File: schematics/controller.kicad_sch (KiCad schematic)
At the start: 48 parts, among them J1 Conn_LoadCell, J2 Conn_Display, J3 Conn_UART, J4 Conn_LiPo, P1 USB-C-6Pin, Q1 MMBT4403, Q2 IRLML6402, SW1 SW_EN, SW2 SW_Boot, SW3 RotaryEncoder_Switch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

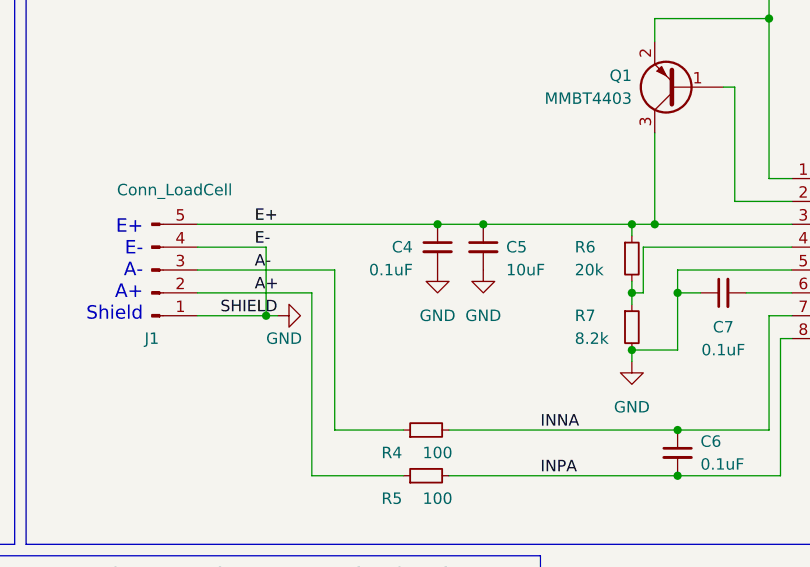
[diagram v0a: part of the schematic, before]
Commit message: Updated voltage divider for hx711 in schematic
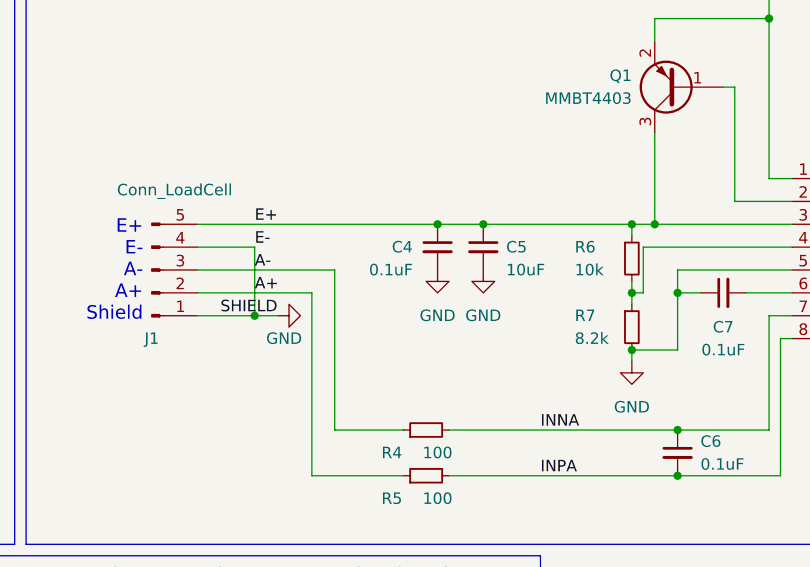
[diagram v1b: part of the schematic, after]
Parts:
- R6: value 20k -> 10k
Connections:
- net A+ is gone; now on net GND: J1.2 (Pin_2), R5.1
- net A- is gone; now on net GND: J1.3 (Pin_3), R4.1
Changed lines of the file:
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@@
   (junction (at 237.49 195.58) (diameter 0) (color 0 0 0 0)
   )
+  (junction (at 214.63 132.08) (diameter 0) (color 0 0 0 0)
+  )
   (junction (at 256.54 129.54) (diameter 0) (color 0 0 0 0)
   )
@@
   )
   (junction (at 308.61 121.92) (diameter 0) (color 0 0 0 0)
-  )
-  (junction (at 215.9 132.08) (diameter 0) (color 0 0 0 0)
   )
   (junction (at 142.24 245.11) (diameter 0) (color 0 0 0 0)
@@
     (stroke (width 0) (type default) (color 0 0 0 0))
   )
+  (wire (pts (xy 214.63 132.08) (xy 217.17 132.08))
+    (stroke (width 0) (type default) (color 0 0 0 0))
+  )
   (polyline (pts (xy 52.07 158.75) (xy 124.46 158.75))
     (stroke (width 0) (type default) (color 0 0 0 0))
@@
     (stroke (width 0) (type default) (color 0 0 0 0))
   )
-  (wire (pts (xy 215.9 132.08) (xy 217.17 132.08))
-    (stroke (width 0) (type default) (color 0 0 0 0))
-  )
   (wire (pts (xy 130.81 234.95) (xy 134.62 234.95))
     (stroke (width 0) (type default) (color 0 0 0 0))
@@
     (stroke (width 0) (type default) (color 0 0 0 0))
   )
-  (wire (pts (xy 215.9 124.46) (xy 215.9 132.08))
+  (wire (pts (xy 214.63 124.46) (xy 214.63 132.08))
     (stroke (width 0) (type default) (color 0 0 0 0))
   )
@@
     (stroke (width 0) (type default) (color 0 0 0 0))
   )
-  (wire (pts (xy 208.28 132.08) (xy 215.9 132.08))
+  (wire (pts (xy 208.28 132.08) (xy 214.63 132.08))
     (stroke (width 0) (type default) (color 0 0 0 0))
   )
@@
     (stroke (width 0) (type default) (color 0 0 0 0))
   )
-  (wire (pts (xy 208.28 124.46) (xy 215.9 124.46))
+  (wire (pts (xy 208.28 124.46) (xy 214.63 124.46))
     (stroke (width 0) (type default) (color 0 0 0 0))
   )
@@
       (effects (font (size 1.27 1.27)) (justify left))
     )
-    (property "Value" "20k" (id 1) (at 250.19 127 0)
+    (property "Value" "10k" (id 1) (at 250.19 127 0)
       (effects (font (size 1.27 1.27)) (justify left))
     )
@@
     )
     (path "/5a71de18-fff9-4a63-b217-7b027e55ea4a"
-      (reference "R6") (unit 1) (value "20k") (footprint "Resistor_SMD:R_0603_1608Metric_Pad0.98x0.95mm_HandSolder")
+      (reference "R6") (unit 1) (value "10k") (footprint "Resistor_SMD:R_0603_1608Metric_Pad0.98x0.95mm_HandSolder")
     )
     (path "/a1a18325-31a1-408b-95d1-26cd10d4dec9"

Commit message: Updated schematic to v1.1.0
* Added TVS diode for USB connector
* Added active buzzer instead of passive piezo buzzer
* Added battery protection IC
* Changed location of enable button, enabling the mounting of a button which is visible externally
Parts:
- removed LS1: Speaker_Crystal, Buzzer_Beeper:MagneticBuzzer_PUI_AT-0927-TT-6-R, symbol Device:Speaker_Crystal
- removed R3: 220, Resistor_SMD:R_0603_1608Metric_Pad0.98x0.95mm_HandSolder, symbol Device:R_Small
- added BZ1: Buzzer, Buzzer_Beeper:Buzzer_12x9.5RM7.6, symbol Device:Buzzer
- added C15: 0.1uF, Capacitor_SMD:C_0603_1608Metric_Pad1.08x0.95mm_HandSolder, symbol Device:C_Small
- added D3: SMAJ6.0CA, Diode_SMD:D_SMA, symbol Device:D_TVS
- added J5: Conn_G13, Connector_Wire:SolderWire-0.5sqmm_1x02_P4.8mm_D0.9mm_OD2.3mm, symbol Connector:Conn_01x02_Male
- added Q3, Q4: IRLML2502, Package_TO_SOT_SMD:SOT-23, symbol Device:Q_NMOS_GSD
- added R15: 2.7k, Resistor_SMD:R_0603_1608Metric_Pad0.98x0.95mm_HandSolder, symbol Device:R_Small
- added R16: 330, Resistor_SMD:R_0603_1608Metric_Pad0.98x0.95mm_HandSolder, symbol Device:R_Small
- added U5: AP9101CK6, Package_TO_SOT_SMD:SOT-23-6, symbol Battery_Management:AP9101CK6
- J4, SW4: footprint Connector_Wire:SolderWire-0.75sqmm_1x02_P7mm_D1.25mm_OD3.5mm -> Connector_Wire:SolderWire-0.5sqmm_1x02_P4.8mm_D0.9mm_OD2.3mm
- renumbered H5 to H1, H6 to H2
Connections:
- net +5V: now also D3.2 (A2)
- net +BATT: now also R16.1
- net GND: now also BZ1.2 (+), D3.1 (A1), J5.1 (Pin_1), Q4.2 (S), R15.1; no longer J4.1 (Pin_1)
- net G13: now reaches U1.16 (IO13)
- net G13: now also J5.2 (Pin_2)
- net at U1.27 (IO16): now also BZ1.1 (-)
- new net: C15.1, R16.2, U5.5 (VDD)
- new net: Q3.3 (D), Q4.3 (D)
- new net -BATT: C15.2, J4.1 (Pin_1), Q3.2 (S), U5.6 (VSS)
- new net CO: Q4.1 (G), U5.3 (CO)
- new net DO: Q3.1 (G), U5.1 (DO)
- new net VM: R15.2, U5.2 (VM)
- no-connect marks 20 -> 19
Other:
- note added: "Battery Protection"
- moved on the sheet: H1, H2, J2, J3

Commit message: Changed circular mounting holes to eliptical for rotary encoder
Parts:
- SW3: footprint Rotary_Encoder:RotaryEncoder_Alps_EC11E-Switch_Vertical_H20mm_CircularMountingHoles -> Rotary_Encoder:RotaryEncoder_Alps_EC11E-Switch_Vertical_H20mm
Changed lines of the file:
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@@
     (property "Reference" "SW3" (id 0) (at 163.83 116.84 0))
     (property "Value" "RotaryEncoder_Switch" (id 1) (at 171.45 119.38 0))
-    (property "Footprint" "Rotary_Encoder:RotaryEncoder_Alps_EC11E-Switch_Vertical_H20mm_CircularMountingHoles" (id 2) (at 147.32 115.316 0)
+    (property "Footprint" "Rotary_Encoder:RotaryEncoder_Alps_EC11E-Switch_Vertical_H20mm" (id 2) (at 147.32 115.316 0)
       (effects (font (size 1.27 1.27)) hide)
     )
@@
     )
     (path "/87dbf7e4-772b-459d-86dc-433bbfeef2ea"
-      (reference "SW3") (unit 1) (value "RotaryEncoder_Switch") (footprint "Rotary_Encoder:RotaryEncoder_Alps_EC11E-Switch_Vertical_H20mm_CircularMountingHoles")
+      (reference "SW3") (unit 1) (value "RotaryEncoder_Switch") (footprint "Rotary_Encoder:RotaryEncoder_Alps_EC11E-Switch_Vertical_H20mm")
     )
     (path "/554bc97c-dda6-441f-adb0-5b318621d6bc"

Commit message: wip
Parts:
- removed R15: 2.7k, Resistor_SMD:R_0603_1608Metric_Pad0.98x0.95mm_HandSolder, symbol Device:R_Small
- removed R16: 330, Resistor_SMD:R_0603_1608Metric_Pad0.98x0.95mm_HandSolder, symbol Device:R_Small
- removed U5: AP9101CK6, Package_TO_SOT_SMD:SOT-23-6, symbol Battery_Management:AP9101CK6
- added R15: 1k, Resistor_SMD:R_0603_1608Metric_Pad0.98x0.95mm_HandSolder, symbol Device:R
- added R3: 100, Resistor_SMD:R_0603_1608Metric_Pad0.98x0.95mm_HandSolder, symbol Device:R
- added U5: DW01-P, Package_TO_SOT_SMD:SOT-23-6_Handsoldering, symbol Custom:DW01-P
- J1: symbol Connector:Conn_01x05_Male -> Connector:Conn_01x05_Pin
- J2: symbol Connector:Conn_01x04_Male -> Connector:Conn_01x04_Pin
- J3: symbol Connector:Conn_01x03_Male -> Connector:Conn_01x03_Pin
- J4, J5: symbol Connector:Conn_01x02_Male -> Connector:Conn_01x02_Pin
- U3: footprint Package_TO_SOT_SMD:SOT-23-5_HandSoldering -> Package_TO_SOT_SMD:SOT-23-5
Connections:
- net +BATT: now also R3.1
- net -BATT: now also U5.6 (GND)
- net GND: now also R15.2
- net at C15.1: now also R3.2, U5.5 (VCC)
- net CO renamed OC
- net OC: now also U5.3 (OC)
- net DO renamed OD
- net OD: now also U5.1 (OD)
- new net: R15.1, U5.2 (CS)
- no-connect marks 19 -> 20
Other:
- moved on the sheet: J4

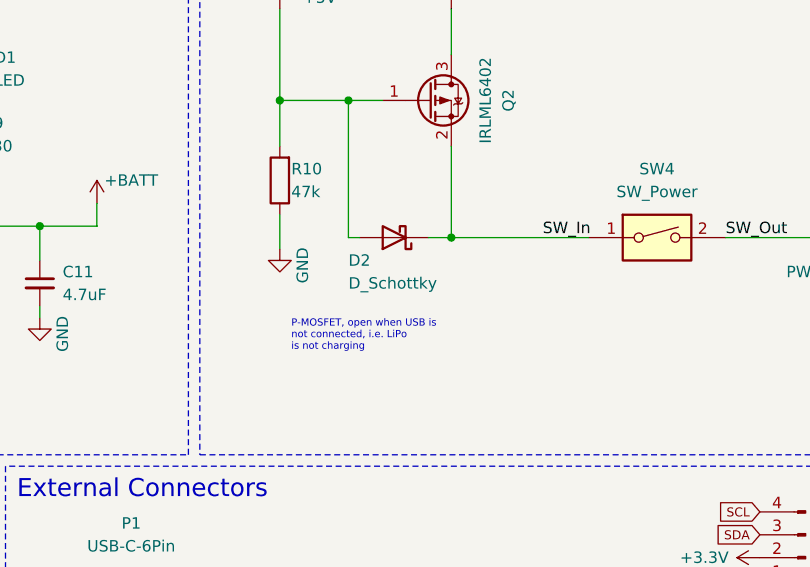
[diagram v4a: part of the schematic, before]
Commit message: Changed lipo protection IC to DW01, added LCSC part numbers
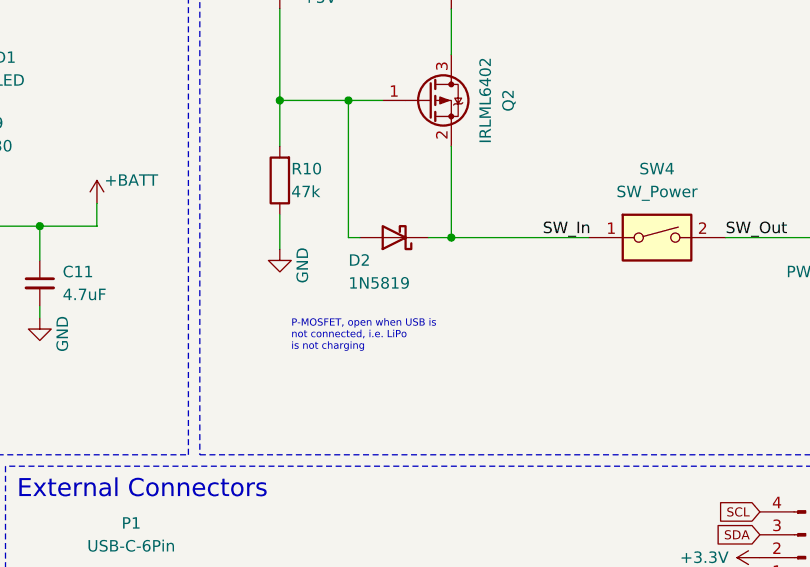
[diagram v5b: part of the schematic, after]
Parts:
- C1, C14, C15, C4, C6, C7, C9: LCSC (none) -> C14663
- C10, C11: LCSC (none) -> C1779
- C12, C13: LCSC (none) -> C28323
- C2, C3, C5, C8: LCSC (none) -> C13585
- D1: LCSC (none) -> C125086
- D2: value D_Schottky -> 1N5819
- Q1: LCSC (none) -> C78864
- Q2: LCSC (none) -> C2593
- Q3, Q4: LCSC (none) -> C5364308
- R1, R2, R6: LCSC (none) -> C25804
- R10, R11, R12: LCSC (none) -> C25819
- R13, R14: LCSC (none) -> C23186
- R15: LCSC (none) -> C21190
- R3, R4, R5: LCSC (none) -> C22775
- R7: LCSC (none) -> C25981
- R8: LCSC (none) -> C22975
- R9: LCSC (none) -> C22808
- U1: LCSC (none) -> C473012
- U2: LCSC (none) -> C6705483
- U3: LCSC (none) -> C424093
- U4: LCSC (none) -> C51118
- U5: LCSC (none) -> C18164398
